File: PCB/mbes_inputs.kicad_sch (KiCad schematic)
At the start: 29 parts, among them Q1 BC337, Q2 BC337, U3 TL084

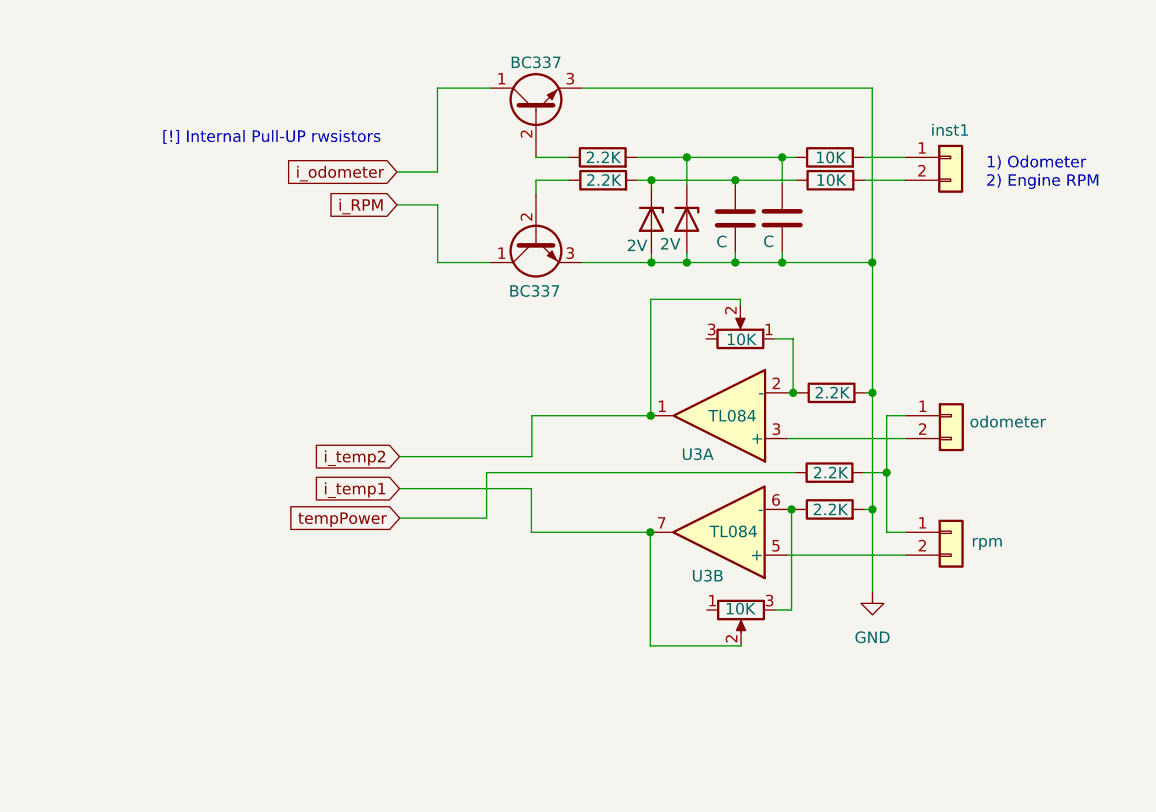
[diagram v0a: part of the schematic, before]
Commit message: Rollback
It will be the last version using DIP. I have to accept it is an old technology, this PCB would be a great result in the 2000 age
but a century quarter is past! :-( It is the SMD age, now. So, after the second upograde of my laboratory,  I will rebuild the
PCB using SMDs.
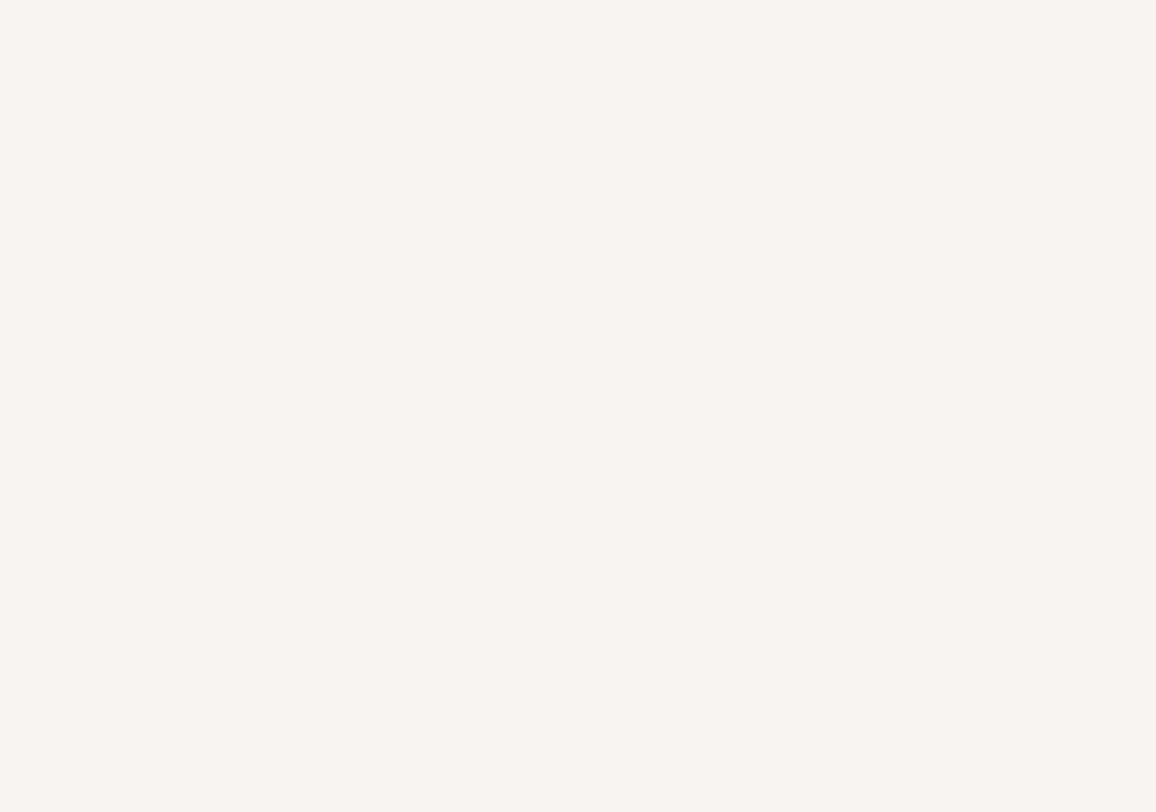
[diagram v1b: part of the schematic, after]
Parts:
- removed C10, C9: C, symbol Device:C
- removed D2, D3: 2V, Diode_SMD:D_SOD-123F, symbol Diode:BZT52Bxx
- removed Q1, Q2: BC337, Package_TO_SOT_THT:TO-92_Inline, symbol Transistor_BJT:BC337
- removed R11, R12: 10K, symbol Device:R
- removed R13, R14, R15, R16, R17: 2.2K, symbol Device:R
- removed RV3, RV4: 10K, Potentiometer_THT:Potentiometer_Bourns_3296W_Vertical, symbol Device:R_Potentiometer
- removed U3: TL084, symbol Amplifier_Operational:TL084
- removed inst1: Conn_01x02, Connector_Wire:SolderWire-0.5sqmm_1x02_P4.6mm_D0.9mm_OD2.1mm, symbol Connector_Generic:Conn_01x02
- removed j?: rpm, Connector_Wire:SolderWire-0.5sqmm_1x02_P4.6mm_D0.9mm_OD2.1mm, symbol Connector_Generic:Conn_01x02
- removed j?: odometer, Connector_Wire:SolderWire-0.5sqmm_1x02_P4.6mm_D0.9mm_OD2.1mm, symbol Connector_Generic:Conn_01x02
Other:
- note removed: "1) Odometer 2) Engine RPM"
- note removed: "[!] Internal Pull-UP rwsistors"

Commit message: Unresolved conflicts after the last marge
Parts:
- added C10, C9: C, symbol Device:C
- added D2, D3: 2V, Diode_SMD:D_SOD-123F, symbol Diode:BZT52Bxx
- added Q1, Q2: BC337, Package_TO_SOT_THT:TO-92_Inline, symbol Transistor_BJT:BC337
- added R11, R12: 10K, symbol Device:R
- added R13, R14, R15, R16: 2.2K, symbol Device:R
- added RV3, RV4: 10K, Potentiometer_THT:Potentiometer_Bourns_3296W_Vertical, symbol Device:R_Potentiometer
- added U3: TL084, symbol Amplifier_Operational:TL084
- added inst1: Conn_01x02, Connector_Wire:SolderWire-0.5sqmm_1x02_P4.6mm_D0.9mm_OD2.1mm, symbol Connector_Generic:Conn_01x02
- added j?: rpm, Connector_Wire:SolderWire-0.5sqmm_1x02_P4.6mm_D0.9mm_OD2.1mm, symbol Connector_Generic:Conn_01x02
- added j?: odometer, Connector_Wire:SolderWire-0.5sqmm_1x02_P4.6mm_D0.9mm_OD2.1mm, symbol Connector_Generic:Conn_01x02
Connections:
- net GND: now also C10.2, C9.2, D2.2 (A), D3.2 (A), Q2.3 (E), R15.2, R16.2
- net tempPower: now also j?.1 (Pin_1), j?.1 (Pin_1)
- new net: C9.1, D2.1 (K), R12.1, R14.2
- new net: R11.2, inst1.1 (Pin_1)
- new net: R12.2, inst1.2 (Pin_2)
- new net: R16.1, U3.2 (-)
- new net: C10.1, D3.1 (K), R11.1, R13.2
- new net: Q1.2 (B), R13.1
- new net: U3.3 (+), j?.2 (Pin_2)
- new net: R15.1, RV4.3, U3.6 (-)
- new net i_RPM: Q2.1 (C)
- new net i_temp1: RV4.2, U3.7
- new net i_temp2: U3.1
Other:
- note added: "1) Odometer 2) Engine RPM"
- note added: "[!] Internal Pull-UP rwsistors"

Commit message: fix
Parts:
- added R17: 2.2K, symbol Device:R
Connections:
- net tempPower: now also R17.1; no longer j?.1 (Pin_1), j?.1 (Pin_1)
- new net: R17.2, j?.1 (Pin_1), j?.1 (Pin_1)
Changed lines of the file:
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@@
   (junction (at 211.0994 94.6912) (diameter 0) (color 0 0 0 0)
   )
-  (junction (at 237.363 87.9856) (diameter 0) (color 0 0 0 0)
-  )
   (junction (at 220.5482 64.7192) (diameter 0) (color 0 0 0 0)
   )
@@
   (junction (at 215.1634 53.0352) (diameter 0) (color 0 0 0 0)
   )
-  (junction (at 235.7882 64.7192) (diameter 0) (color 0 0 0 0)
+  (junction (at 235.7628 64.7192) (diameter 0) (color 0 0 0 0)
   )
   (junction (at 211.1502 81.7372) (diameter 0) (color 0 0 0 0)
@@
   )
   (junction (at 78.232 135.89) (diameter 0) (color 0 0 0 0)
+  )
+  (junction (at 237.363 88.0618) (diameter 0) (color 0 0 0 0)
   )
   (junction (at 211.2264 64.7192) (diameter 0) (color 0 0 0 0)
@@
     (stroke (width 0) (type default))
   )
-  (wire (pts (xy 237.363 94.6912) (xy 237.363 87.9856))
+  (wire (pts (xy 237.363 94.6912) (xy 237.363 88.0618))
     (stroke (width 0) (type default))
   )
@@
     (stroke (width 0) (type default))
   )
-  (wire (pts (xy 235.7374 53.0352) (xy 239.395 53.0352))
+  (wire (pts (xy 234.8738 53.0352) (xy 239.395 53.0352))
     (stroke (width 0) (type default))
   )
@@
     (stroke (width 0) (type default))
   )
-  (wire (pts (xy 192.913 93.1164) (xy 192.913 87.9856))
+  (wire (pts (xy 192.913 93.1164) (xy 192.913 88.0618))
     (stroke (width 0) (type default))
   )
@@
     (stroke (width 0) (type default))
   )
-  (wire (pts (xy 220.5482 55.5752) (xy 228.1682 55.5752))
+  (wire (pts (xy 220.5482 55.5752) (xy 227.3046 55.5752))
     (stroke (width 0) (type default))
   )
@@
     (stroke (width 0) (type default))
   )
-  (wire (pts (xy 237.5154 45.339) (xy 237.5154 64.7192))
+  (wire (pts (xy 235.7628 45.339) (xy 235.7628 64.7192))
     (stroke (width 0) (type default))
   )
@@
     (stroke (width 0) (type default))
   )
-  (wire (pts (xy 225.7552 53.0352) (xy 228.1174 53.0352))
+  (wire (pts (xy 225.7552 53.0352) (xy 227.2538 53.0352))
     (stroke (width 0) (type default))
   )
@@
     (stroke (width 0) (type default))
   )
-  (wire (pts (xy 235.7882 64.7192) (xy 237.5154 64.7192))
-    (stroke (width 0) (type default))
-  )
   (wire (pts (xy 61.976 114.3) (xy 77.978 114.3))
     (stroke (width 0) (type default))
@@
     (stroke (width 0) (type default))
   )
-  (wire (pts (xy 235.7882 55.5752) (xy 239.395 55.5752))
+  (wire (pts (xy 234.9246 55.5752) (xy 239.395 55.5752))
     (stroke (width 0) (type default))
   )
@@
     (stroke (width 0) (type default))
   )
-  (wire (pts (xy 192.913 87.9856) (xy 237.363 87.9856))
+  (wire (pts (xy 192.913 88.0618) (xy 227.203 88.0618))
     (stroke (width 0) (type default))
   )
@@
     (stroke (width 0) (type default))
   )
-  (wire (pts (xy 237.363 87.9856) (xy 237.363 81.7372))
+  (wire (pts (xy 237.363 81.7372) (xy 237.363 88.0618))
     (stroke (width 0) (type default))
   )
@@
     (stroke (width 0) (type default))
   )
-  (wire (pts (xy 203.5048 45.339) (xy 237.5154 45.339))
+  (wire (pts (xy 203.5048 45.339) (xy 235.7628 45.339))
     (stroke (width 0) (type default))
   )
@@
     (stroke (width 0) (type default))
   )
-  (wire (pts (xy 225.7552 64.7192) (xy 235.7882 64.7192))
+  (wire (pts (xy 225.7552 64.7192) (xy 235.7628 64.7192))
+    (stroke (width 0) (type default))
+  )
+  (wire (pts (xy 234.823 88.0618) (xy 237.363 88.0618))
     (stroke (width 0) (type default))
   )
@@
   )
   (wire (pts (xy 235.7882 79.1972) (xy 235.7882 64.7192))
+    (stroke (width 0) (type default))
+  )
+  (wire (pts (xy 235.7628 64.7192) (xy 235.7882 64.7192))
     (stroke (width 0) (type default))
   )
@@
     )
   )
+  (symbol (lib_id "Device:R") (at 231.013 88.0618 90) (unit 1)
+    (in_bom yes) (on_board yes) (dnp no)
+    (property "Reference" "R17" (at 231.013 82.1182 90)
+      (effects (font (size 1.27 1.27)) hide)
+    )
+    (property "Value" "2.2K" (at 231.1146 88.1126 90)
+      (effects (font (size 1.27 1.27)))
+    )
+    (property "Footprint" "" (at 231.013 89.8398 90)
+      (effects (font (size 1.27 1.27)) hide)
+    )
+    (property "Datasheet" "~" (at 231.013 88.0618 0)
+      (effects (font (size 1.27 1.27)) hide)
+    )
+    (pin "2")
+    (pin "1")
+    (instances
+      (project "pcb-a"
+        (path "/709d0967-afe5-49d3-92a5-d2bb94550bdb/0b22d592-b723-42a2-89dd-bec665c2bd26"
+          (reference "R17") (unit 1)
+        )
+      )
+    )
+  )
   (symbol (lib_id "Device:C") (at 220.5482 59.817 0) (unit 1)
     (in_bom yes) (on_board yes) (dnp no)
@@
     )
   )
-  (symbol (lib_id "Device:R") (at 231.9274 53.0352 90) (unit 1)
-    (in_bom yes) (on_board yes) (dnp no)
-    (property "Reference" "R11" (at 231.9274 47.0916 90)
-      (effects (font (size 1.27 1.27)) hide)
-    )
-    (property "Value" "10K" (at 231.9782 53.086 90)
-      (effects (font (size 1.27 1.27)))
-    )
-    (property "Footprint" "" (at 231.9274 54.8132 90)
-      (effects (font (size 1.27 1.27)) hide)
-    )
-    (property "Datasheet" "~" (at 231.9274 53.0352 0)
+  (symbol (lib_id "Device:R") (at 231.0638 53.0352 90) (unit 1)
+    (in_bom yes) (on_board yes) (dnp no)
+    (property "Reference" "R11" (at 231.0638 47.0916 90)
+      (effects (font (size 1.27 1.27)) hide)
+    )
+    (property "Value" "10K" (at 231.1146 53.086 90)
+      (effects (font (size 1.27 1.27)))
+    )
+    (property "Footprint" "" (at 231.0638 54.8132 90)
+      (effects (font (size 1.27 1.27)) hide)
+    )
+    (property "Datasheet" "~" (at 231.0638 53.0352 0)
       (effects (font (size 1.27 1.27)) hide)
     )
@@
     )
   )
-  (symbol (lib_id "Device:R") (at 231.9782 55.5752 90) (unit 1)
-    (in_bom yes) (on_board yes) (dnp no)
-    (property "Reference" "R12" (at 231.9782 49.6316 90)
-      (effects (font (size 1.27 1.27)) hide)
-    )
-    (property "Value" "10K" (at 232.029 55.6006 90)
-      (effects (font (size 1.27 1.27)))
-    )
-    (property "Footprint" "" (at 231.9782 57.3532 90)
-      (effects (font (size 1.27 1.27)) hide)
-    )
-    (property "Datasheet" "~" (at 231.9782 55.5752 0)
-      (effects (font (size 1.27 1.27)) hide)
-    )
+  (symbol (lib_id "Device:R") (at 231.1146 55.5752 90) (unit 1)
+    (in_bom yes) (on_board yes) (dnp no)
+    (property "Reference" "R12" (at 231.1146 49.6316 90)
+      (effects (font (size 1.27 1.27)) hide)
+    )
+    (property "Value" "10K" (at 231.1654 55.6006 90)
+      (effects (font (size 1.27 1.27)))
+    )
+    (property "Footprint" "" (at 231.1146 57.3532 90)
+      (effects (font (size 1.27 1.27)) hide)
+    )
+    (property "Datasheet" "~" (at 231.1146 55.5752 0)
+      (effects (font (size 1.27 1.27)) hide)
+    )
